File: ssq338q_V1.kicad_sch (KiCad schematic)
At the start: 50 parts, among them J4 Conn_01x04_MountingPin, J6 Conn_01x06_MountingPin, J7 Conn_01x03_MountingPin, J8 Conn_01x02_MountingPin, U11 W25Q128JVSIQ, U13 BL-M8812EU2, U2 SSC338Q, X2 24MHz

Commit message: 24_09_26
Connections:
- net USB_DM renamed USB_DN
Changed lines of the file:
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@@
 		)
 	)
-	(label "USB_DM"
+	(label "USB_DN"
 		(at 306.07 232.41 90)
 		(effects
@@
 		)
 	)
-	(label "USB_DM"
+	(label "USB_DN"
 		(at 209.55 87.63 180)
 		(effects

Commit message: traces done
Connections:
- net FUART_RX: now also J4.3 (Pin_3)
- net FUART_TX: now also J4.4 (Pin_4)
- net UART_RX1: no longer J4.3 (Pin_3)
- net UART_TX1: no longer J4.4 (Pin_4)
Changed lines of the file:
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@@
 	(wire
 		(pts
-			(xy 374.65 130.81) (xy 383.54 130.81)
+			(xy 361.95 130.81) (xy 383.54 130.81)
 		)
 		(stroke
@@
 	(wire
 		(pts
-			(xy 374.65 133.35) (xy 383.54 133.35)
+			(xy 361.95 133.35) (xy 383.54 133.35)
 		)
 		(stroke
@@
 		)
 	)
+	(label "FUART_RX"
+		(at 361.95 130.81 0)
+		(effects
+			(font
+				(size 1.2446 1.2446)
+			)
+			(justify left bottom)
+		)
+	)
 	(label "MIPI_CK+"
 		(at 29.21 222.25 0)
@@
 		)
 	)
+	(label "FUART_TX"
+		(at 361.95 133.35 0)
+		(effects
+			(font
+				(size 1.2446 1.2446)
+			)
+			(justify left bottom)
+		)
+	)
 	(label "MIPI_CK-"
 		(at 29.21 224.79 0)
@@
 		)
 	)
-	(label "UART_TX1"
-		(at 374.65 133.35 180)
-		(effects
-			(font
-				(size 1.2446 1.2446)
-			)
-			(justify right bottom)
-		)
-	)
 	(label "ETH_LED1"
 		(at 29.21 186.69 0)
@@
 		)
 	)
-	(label "UART_RX1"
-		(at 374.65 130.81 180)
-		(effects
-			(font
-				(size 1.2446 1.2446)
-			)
-			(justify right bottom)
-		)
-	)

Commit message: minor changes and prepared BOM
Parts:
- C41, C77: LCSC Part Name 10uF ±20% 25V -> (none)
- C42, C78, C79, C80, C81, C82, C86, C87: LCSC Part Name 100nF ±10% 50V -> (none)
- DF2: LCSC Part Name DF56C-26S-0.3V(51) -> taobao
- FB1, FB2: now left out of the parts list
- R21, R22, R65, R74: value 10K -> 10k
- U13, U2: LCSC Part Name (none) -> taobao
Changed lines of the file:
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@@
 			)
 		)
-		(property "LCSC Part Name" "100nF ±10% 50V"
+		(property "LCSC Part Name" ""
 			(at 331.47 127 0)
 			(hide yes)
@@
 		(body_style 1)
 		(exclude_from_sim no)
-		(in_bom yes)
+		(in_bom no)
 		(on_board yes)
 		(in_pos_files yes)
@@
 			)
 		)
-		(property "LCSC Part Name" "100nF ±10% 50V"
+		(property "LCSC Part Name" ""
 			(at 110.49 62.23 0)
 			(hide yes)
@@
 			)
 		)
-		(property "LCSC Part Name" "100nF ±10% 50V"
+		(property "LCSC Part Name" ""
 			(at 46.99 63.5 0)
 			(hide yes)
@@
 			)
 		)
-		(property "LCSC Part Name" "100nF ±10% 50V"
+		(property "LCSC Part Name" ""
 			(at 196.85 168.91 0)
 			(hide yes)
@@
 			)
 		)
-		(property "LCSC Part Name" "10uF ±20% 25V"
+		(property "LCSC Part Name" ""
 			(at 36.83 87.63 0)
 			(hide yes)
@@
 			)
 		)
-		(property "LCSC Part Name" "100nF ±10% 50V"
+		(property "LCSC Part Name" ""
 			(at 62.23 66.04 0)
 			(hide yes)
@@
 			)
 		)
-		(property "LCSC Part Name" "DF56C-26S-0.3V(51)"
+		(property "LCSC Part Name" "taobao"
 			(at 280.67 50.8 0)
 			(hide yes)
@@
 			)
 		)
-		(property "LCSC Part Name" "10uF ±20% 25V"
+		(property "LCSC Part Name" ""
 			(at 41.91 63.5 0)
 			(hide yes)
@@
 			)
 		)
-		(property "LCSC Part Name" "100nF ±10% 50V"
+		(property "LCSC Part Name" ""
 			(at 365.76 60.96 0)
 			(hide yes)
@@
 			)
 		)
-		(property "Value" "10K"
+		(property "Value" "10k"
 			(at 344.17 53.34 90)
 			(show_name no)
@@
 		(body_style 1)
 		(exclude_from_sim no)
-		(in_bom yes)
+		(in_bom no)
 		(on_board yes)
 		(in_pos_files yes)
@@
 			)
 		)
-		(property "Value" "10K"
+		(property "Value" "10k"
 			(at 218.44 128.27 90)
 			(show_name no)
@@
 			)
 		)
-		(property "Value" "10K"
+		(property "Value" "10k"
 			(at 334.01 53.34 90)
 			(show_name no)
@@
 			)
 		)
+		(property "LCSC Part Name" "taobao"
+			(at 311.15 196.85 0)
+			(hide yes)
+			(show_name no)
+			(do_not_autoplace no)
+			(effects
+				(font
+					(size 1.27 1.27)
+				)
+			)
+		)
 		(pin "13"
 		)
@@
 			)
 		)
+		(property "LCSC Part Name" "taobao"
+			(at 102.87 128.27 0)
+			(hide yes)
+			(show_name no)
+			(do_not_autoplace no)
+			(effects
+				(font
+					(size 1.27 1.27)
+				)
+			)
+		)
 		(pin "7"
 		)
@@
 			)
 		)
-		(property "LCSC Part Name" "100nF ±10% 50V"
+		(property "LCSC Part Name" ""
 			(at 215.9 135.89 0)
 			(hide yes)
@@
 			)
 		)
-		(property "Value" "10K"
+		(property "Value" "10k"
 			(at 323.85 44.45 90)
 			(show_name no)
@@
 			)
 		)
-		(property "LCSC Part Name" "100nF ±10% 50V"
+		(property "LCSC Part Name" ""
 			(at 137.16 59.69 0)
 			(hide yes)

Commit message: bom + alternative camera version copy
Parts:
- DF2: LCSC Part Name taobao -> C5338332
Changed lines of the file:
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@@
 			)
 		)
-		(property "LCSC Part Name" "taobao"
+		(property "LCSC Part Name" "C5338332"
 			(at 280.67 50.8 0)
 			(hide yes)

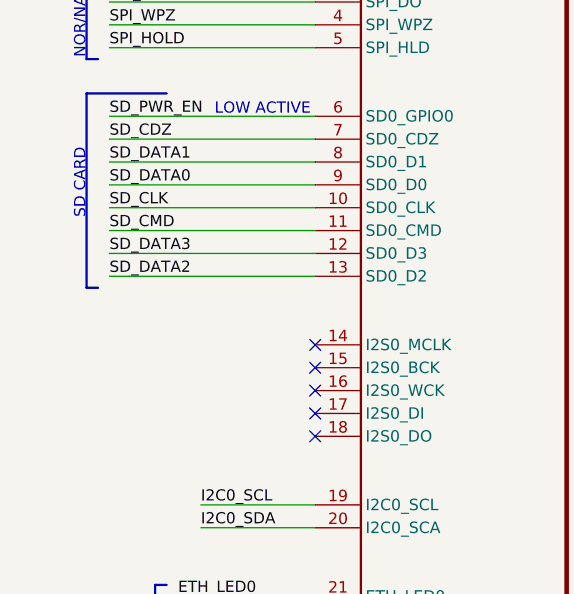
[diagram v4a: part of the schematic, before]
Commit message: sd pullup, finilized design
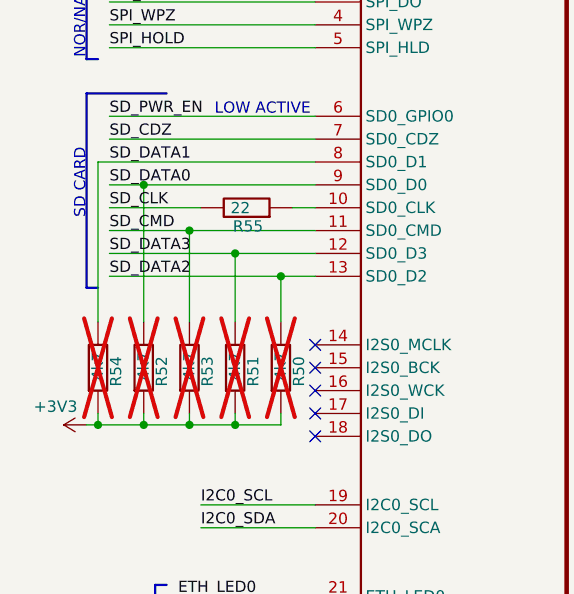
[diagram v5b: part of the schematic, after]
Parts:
- added R50, R51, R52, R53, R54: 4k7, Resistor_SMD:R_0402_1005Metric, symbol ProPrj_Ope-easyedapro:电阻
- added R55: 22, Resistor_SMD:R_0402_1005Metric, symbol ProPrj_Ope-easyedapro:电阻
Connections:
- net +3V3: now also R50.1, R51.1, R52.1, R53.1, R54.1
- net SD_CLK: now also R55.2; no longer U2.10 (SD0_CLK)
- net SD_CMD: now also R53.2
- net SD_DATA0: now also R52.2
- net SD_DATA1: now also R54.2
- net SD_DATA2: now also R50.2
- net SD_DATA3: now also R51.2
- new net: R55.1, U2.10 (SD0_CLK)
